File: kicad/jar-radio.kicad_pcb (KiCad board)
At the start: 2 copper layers, 85.5 x 85.5 mm, 65 parts, among them J1 USB-C 5V, J2 BATT (PH), J3 ANT (XH), J4 SPK (XH), Q1 AO3401A, U1 Si4825-A10, U2 NS8002, U3 TP4056, U4 XC6206P332MR, U5 XC61CN2702MR, Y1 32.768kHz

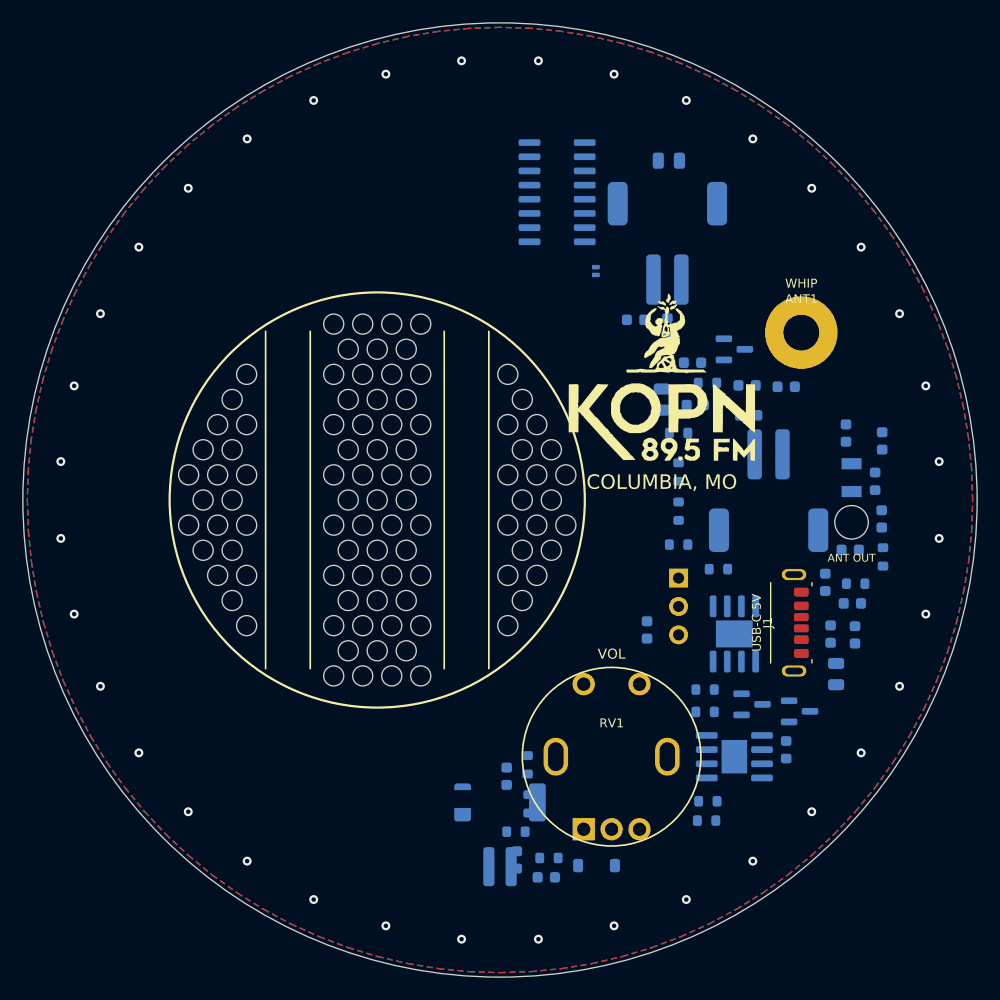
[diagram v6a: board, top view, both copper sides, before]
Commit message: Rev B layout: all parts on the top face, speaker down / holder up, new grille, speaker and holder outlines (placed, routing in progress)
Co-Authored-By: Claude Opus 5.5 <noreply@anthropic.com>
Claude-Session: https://claude.ai/code/session_01UChZ4MGw6SzykNSB399iC4
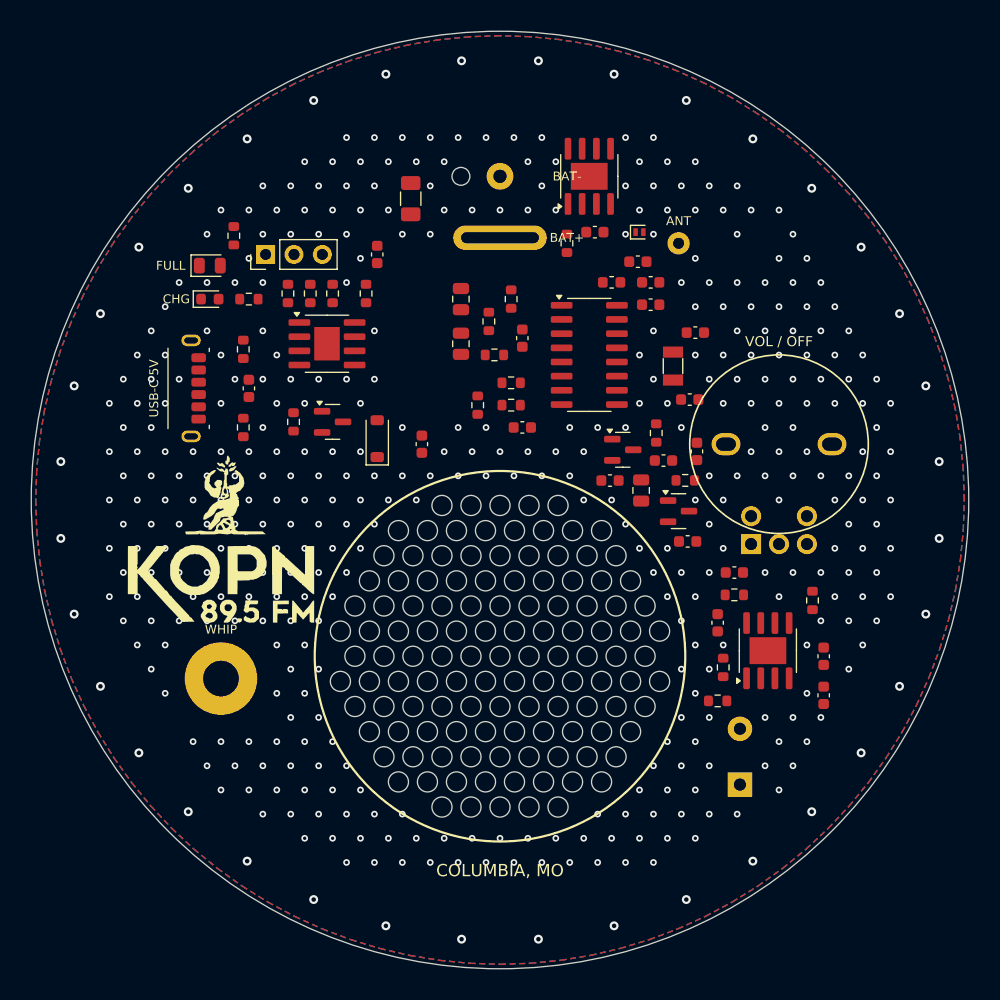
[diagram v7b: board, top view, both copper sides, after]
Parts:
- removed MK6: ZipTie_Slot_4x1.6, jar-radio:ZipTie_Slot_4x1.6
- removed MK7: Antenna_Wire_Exit_D3.0, jar-radio:Antenna_Wire_Exit_D3.0
- removed MK8: Logo_KOPN_15mm, jar-radio:Logo_KOPN_15mm
- removed MK9: Logo_CGW_14mm, jar-radio:Logo_CGW_14mm
- added C22: 100nF, Capacitor_SMD:C_0603_1608Metric, F.Cu at (158.5, 76.0)
- added F1: 0R (PTC spot), Fuse:Fuse_1206_3216Metric, F.Cu at (142.0, 73.0)
- added R17: 100k, Resistor_SMD:R_0603_1608Metric, F.Cu at (151.0, 91.5)
- added R18: 1k, Resistor_SMD:R_0603_1608Metric, F.Cu at (156.0, 77.0)
- added R20: 5.1k (DNP), Resistor_SMD:R_0603_1608Metric, F.Cu at (133.0, 81.5)
- added R21: 0R, Resistor_SMD:R_0603_1608Metric, F.Cu at (131.0, 81.5)
- added R22: 4.7k, Resistor_SMD:R_0603_1608Metric, F.Cu at (166.6, 98.2)
- added RT1: NTC 10k B3950 (DNP), Resistor_SMD:R_0603_1608Metric, F.Cu at (135.0, 81.5)
- added U6: XB8089D, Package_SO:SOIC-8-1EP_3.9x4.9mm_P1.27mm_EP2.41x3.3mm, F.Cu at (158.0, 71.0)
- C1, C10, C11, C12, C13, C14, C15, C16, C17, C18, C19, C2, C20, C21, C3, C4, C5, C6, C7, C8, D1, D2, L1, Q1, R1, R10, R11, R12, R14, R16, R2, R3, R4, R6, R7, R9, RV2, U1, U2, U3, U4, U5, Y1: moved to F.Cu
- C9: value 1nF C0G -> 1nF; moved to F.Cu
- D3: footprint LED_SMD:LED_0603_1608Metric -> LED_SMD:LED_0805_2012Metric; moved to F.Cu
- D4: value ESD <=1pF -> ESD 0.5pF; moved to F.Cu
- J1: footprint jar-radio:USB_C_Receptacle_ShouHan_TYPE-C-6PLTH6.8-DJ_Vertical -> jar-radio:USB_C_Receptacle_ShouHan_TYPE-C-6P-LTH6.8-108_Vertical
- J2: value BATT (PH) -> 18650 holder; footprint Connector_JST:JST_PH_S2B-PH-SM4-TB_1x02-1MP_P2.00mm_Horizontal -> jar-radio:Battery_Holder_Tab_Slot_Plus_Wire; moved to F.Cu
- J3: value ANT (XH) -> ANT wire; footprint jar-radio:Connector_XH-SMD_GSwitch_GT-A2501WRS-102_1x02_P2.50mm_Horizontal -> jar-radio:Antenna_Wire_Solder_D1.0; moved to F.Cu
- J4: value SPK (XH) -> SPK wires; footprint jar-radio:Connector_XH-SMD_GSwitch_GT-A2501WRS-102_1x02_P2.50mm_Horizontal -> jar-radio:Speaker_Wire_Pads_P5; moved to F.Cu
- MK1: value Speaker_D49_Keepout -> Speaker_D40_Outline; footprint jar-radio:Speaker_D49_Keepout -> jar-radio:Speaker_D40_Outline
- MK2: value Speaker_Grille_D36_2Bars -> Speaker_Grille_D32; footprint jar-radio:Speaker_Grille_D36_2Bars -> jar-radio:Speaker_Grille_D32
- MK3: value ZipTie_Slot_4x1.6 -> Holder_18650_EndFace_Outline; footprint jar-radio:ZipTie_Slot_4x1.6 -> jar-radio:Holder_18650_EndFace_Outline; moved to B.Cu
- MK4: value ZipTie_Slot_4x1.6 -> Logo_KOPN_15mm; footprint jar-radio:ZipTie_Slot_4x1.6 -> jar-radio:Logo_KOPN_15mm
- MK5: value ZipTie_Slot_4x1.6 -> Logo_CGW_14mm; footprint jar-radio:ZipTie_Slot_4x1.6 -> jar-radio:Logo_CGW_14mm; moved to B.Cu
- R13: value 3.0k -> 2.4k; moved to F.Cu
- R15: value 2.2k -> 1k; moved to F.Cu
- R5: value 430k -> 330k; moved to F.Cu
- R8: value 560k -> 680k; moved to F.Cu
- RV1: value 20k + SW -> 10k A + SW; footprint jar-radio:Potentiometer_RV097NS_Switch_Vertical_PROVISIONAL -> jar-radio:Potentiometer_CTR_R09512NS_RearMount_Switch
- moved D3 67.4 mm to (124.0, 79.0), turned to 0 degrees
- moved D2 61.8 mm to (124.0, 82.0), turned to 0 degrees
- moved ANT1 60.5 mm to (125.0, 116.0)
- moved R12 60.3 mm to (127.0, 86.5)
- moved J1 57.9 mm to (123.0, 90.0)
- moved C15 57.9 mm to (127.5, 90.0)
- moved C16 57.8 mm to (139.0, 78.0), turned to 90 degrees
- moved R15 57.3 mm to (126.1, 76.3)
- moved R11 56.6 mm to (127.0, 93.5), turned to 90 degrees
- moved J2 53.5 mm to (150.0, 76.5), turned to 180 degrees
- moved R13 53.2 mm to (138.0, 81.5), turned to 90 degrees
- moved U3 52.0 mm to (134.5, 86.0), turned to 0 degrees
- moved Q1 49.2 mm to (135.0, 93.0)
- moved R14 48.6 mm to (127.5, 82.0), turned to 0 degrees
- moved RV2 47.0 mm to (129.0, 78.0), turned to 90 degrees
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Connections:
- C10 pad 2: VOL_TOP -> AOUT_C
- J2 pad 1: VBAT -> BAT_P
- J2 pad 2: GND -> BAT_N
- R5 pad 2: BAND -> BAND_M
- U3 pad 1: GND -> TEMP
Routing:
- net GND: vias 36 -> 424
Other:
- board size 85.5 x 85.5 mm -> 84 x 84 mm
- board text added: "CERN-OHL-S-2.0"
- board text added: "CHG"
- board text added: "FULL"
- board text added: "KOPN 89.5 JAR RADIO rev B"
- board text added: "Li-ion 18650 inside: protected cell only"
- board text added: "after The Public Radio"
- board text removed: "ANTENNA"
- board text removed: "BATT +/-"
- board text removed: "CERN-OHL-S-2.0 after The Public Radio"
- board text removed: "KOPN 89.5 JAR RADIO rev A"
- board text removed: "SPEAKER"

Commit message: Board rev B: all-top-side layout routed (0 unconnected, 0 clearance), JLC gerbers/BOM/CPL, renders, maze-router + GND island fixes in the route pipeline
Co-Authored-By: Claude Opus 5.5 <noreply@anthropic.com>
Claude-Session: https://claude.ai/code/session_01UChZ4MGw6SzykNSB399iC4
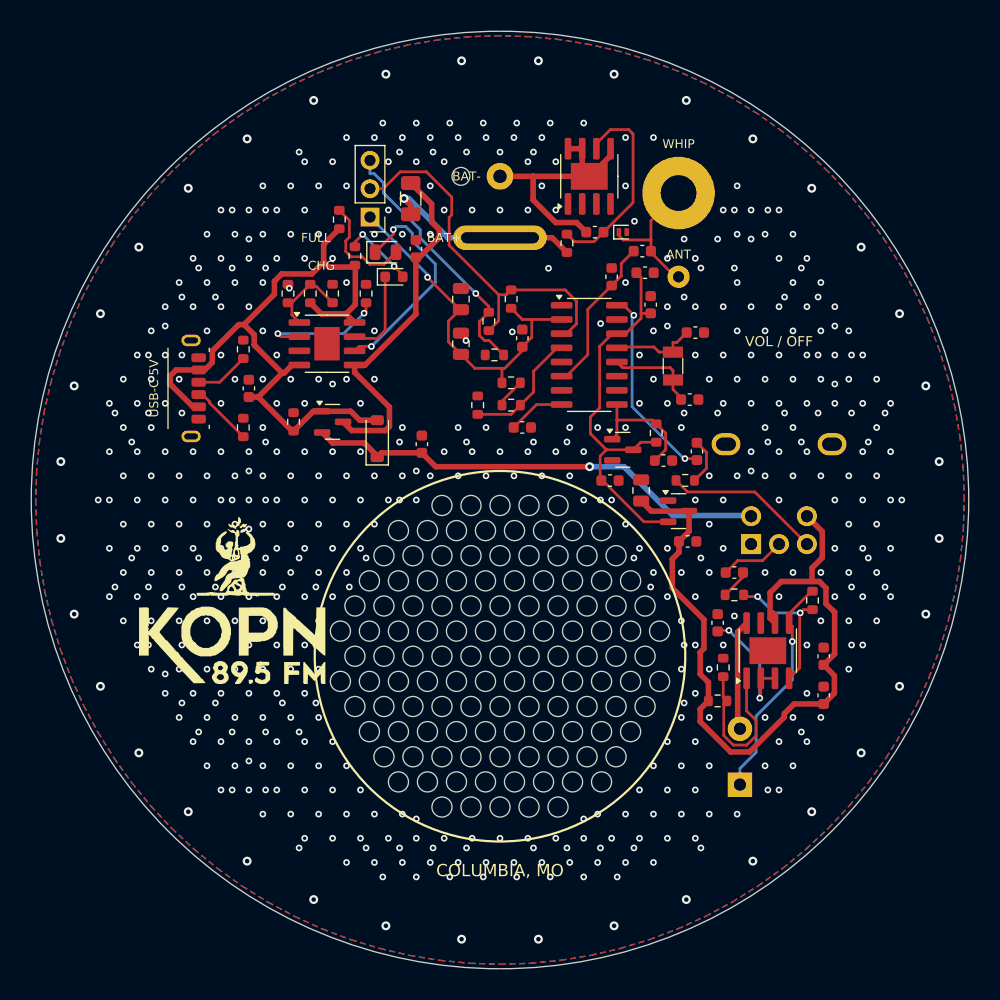
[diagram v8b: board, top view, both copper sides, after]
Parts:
- moved ANT1 59.8 mm to (166.0, 72.5)
- moved D2 16.6 mm to (140.5, 80.0)
- moved D3 15.8 mm to (139.8, 77.8)
- moved R14 10.3 mm to (137.0, 78.1), turned to 90 degrees
- moved RV2 9.94 mm to (138.4, 74.6), turned to 180 degrees
- moved R15 9.56 mm to (135.6, 74.9)
- moved MK4 5.59 mm to (126.0, 109.0)
- moved C16 3.50 mm to (142.5, 77.5)
- moved J3 3.00 mm to (166.0, 80.0)
- moved D4 1.50 mm to (161.0, 76.0)
- moved C9 1.03 mm to (162.8, 77.7)
- moved C4 1.00 mm to (163.0, 79.6)
- moved L1 0.50 mm to (160.0, 80.0), turned to 90 degrees
- turned C3 to 90 degrees
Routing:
- net VSW: track 0.00 -> 67.5 mm
- net VBUS: track 0.00 -> 63.8 mm
- net VSYS: track 0.00 -> 41.9 mm, vias 0 -> 1
- net +3V3: track 0.00 -> 35.4 mm
- net TUNE2: track 0.00 -> 34.4 mm
- net TUNE1: track 0.00 -> 32.7 mm, vias 0 -> 1
- net VBAT: track 0.00 -> 32.7 mm
- net TUNE_LO: track 0.00 -> 23.6 mm, vias 0 -> 1
- net BAT_N: track 0.00 -> 23.0 mm
- net SPK+: track 0.00 -> 20.3 mm, vias 0 -> 1
- net STDBY: track 0.00 -> 19.8 mm, vias 0 -> 2
- net BAT_P: track 0.00 -> 18.3 mm, vias 0 -> 1
- net XB_VDD: track 0.00 -> 18.2 mm
- net AOUT: track 0.00 -> 17.9 mm, vias 0 -> 2
- net AMP_SD: track 0.00 -> 14.6 mm
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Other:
- board text added: "BAT+"
- board text added: "BAT-"
- board text added: "PROTECTED 18650 ONLY"
- board text removed: "Li-ion 18650 inside: protected cell only"
